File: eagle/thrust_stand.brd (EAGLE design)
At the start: 100 x 80 mm, 28 parts, among them IC1 7805TV, Q1 16Mhz, Q2 IRF510, T1 2N3904, U2 ATMEGA328P_PDIP

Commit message: routed
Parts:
- moved LED1 2.62 mm to (66.7, 34.3), turned to 90 degrees
- moved BATTERY 2.54 mm to (62.2, 48.3)
- moved R2 2.29 mm to (64.1, 27.9)
- moved IGNITER 1.80 mm to (67.3, 12.7), turned to 270 degrees
- moved Q2 1.27 mm to (64.8, 16.5)
- moved R24 1.27 mm to (26.7, 24.1)
- moved BUTTON 1.27 mm to (53.3, 41.9)
- moved R1 0.63 mm to (36.8, 48.9)
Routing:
- net GND: track 63.5 -> 227.3 mm, vias 0 -> 2
- net +5V: track 26.4 -> 129.3 mm, vias 0 -> 2
- net +9V: track 0.00 -> 38.9 mm
- net N$24: track 0.00 -> 17.9 mm
- net N$4: track 0.00 -> 17.3 mm
- net N$5: track 0.00 -> 16.5 mm
- net N$12: track 0.00 -> 12.5 mm
- net N$15: track 0.00 -> 11.2 mm
- net N$3: track 0.00 -> 10.7 mm
- net N$6: track 0.00 -> 10.7 mm
- net N$43: track 0.00 -> 8.35 mm
- net N$13: track 0.00 -> 6.13 mm
- net N$16: track 0.00 -> 5.61 mm
- net N$21: track 0.00 -> 5.46 mm
- net N$14: track 0.00 -> 3.18 mm
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
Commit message: tweaks
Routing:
- net N$7: track 41.8 -> 39.7 mm
- net GND: track 227.3 -> 226.8 mm
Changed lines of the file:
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@@
 <wire x1="30.48" y1="30.48" x2="30.48" y2="33.02" width="0.8128" layer="16"/>
 <wire x1="30.48" y1="33.02" x2="36.83" y2="33.02" width="0.8128" layer="16"/>
-<wire x1="53.34" y1="46.99" x2="55.88" y2="46.99" width="0.8128" layer="16"/>
-<wire x1="55.88" y1="46.99" x2="59.69" y2="43.18" width="0.8128" layer="16"/>
+<wire x1="53.34" y1="46.99" x2="55.88" y2="46.99" width="1.016" layer="16"/>
+<wire x1="55.88" y1="46.99" x2="59.69" y2="43.18" width="1.016" layer="16"/>
 <wire x1="36.83" y1="52.705" x2="21.59" y2="52.705" width="0.8128" layer="16"/>
 <wire x1="21.59" y1="52.705" x2="13.97" y2="45.085" width="0.8128" layer="16"/>
@@
 <wire x1="48.26" y1="31.75" x2="46.99" y2="31.75" width="0.8128" layer="16"/>
 <wire x1="46.99" y1="31.75" x2="43.18" y2="29.21" width="0.8128" layer="16"/>
-<wire x1="43.18" y1="29.21" x2="43.18" y2="12.7" width="0.8128" layer="16"/>
-<wire x1="43.18" y1="12.7" x2="45.72" y2="11.43" width="0.8128" layer="16"/>
+<wire x1="43.18" y1="29.21" x2="43.18" y2="13.97" width="0.8128" layer="16"/>
+<wire x1="43.18" y1="13.97" x2="45.72" y2="11.43" width="0.8128" layer="16"/>
 <wire x1="45.72" y1="11.43" x2="52.07" y2="11.43" width="0.8128" layer="16"/>
 <wire x1="52.07" y1="11.43" x2="55.88" y2="13.97" width="0.8128" layer="16"/>
@@
 <contactref element="IGNITER" pad="TP-2"/>
 <wire x1="43.18" y1="29.21" x2="40.64" y2="29.21" width="0.8128" layer="16"/>
-<wire x1="53.34" y1="49.53" x2="57.15" y2="49.53" width="0.8128" layer="16"/>
-<wire x1="57.15" y1="49.53" x2="60.96" y2="48.26" width="0.8128" layer="16"/>
+<wire x1="53.34" y1="49.53" x2="57.15" y2="49.53" width="1.016" layer="16"/>
+<wire x1="57.15" y1="49.53" x2="60.96" y2="48.26" width="1.016" layer="16"/>
 <wire x1="24.13" y1="16.51" x2="25.4" y2="17.78" width="0.8128" layer="16"/>
 <wire x1="25.4" y1="17.78" x2="29.21" y2="17.78" width="0.8128" layer="16"/>
@@
 <wire x1="27.94" y1="40.64" x2="26.67" y2="39.37" width="0.8128" layer="16"/>
 <wire x1="26.67" y1="39.37" x2="26.67" y2="30.48" width="0.8128" layer="16"/>
-<wire x1="60.96" y1="48.26" x2="60.96" y2="46.355" width="0.8128" layer="16"/>
-<wire x1="60.96" y1="46.355" x2="62.23" y2="45.085" width="0.8128" layer="16"/>
-<wire x1="62.23" y1="45.085" x2="62.23" y2="43.18" width="0.8128" layer="16"/>
-<wire x1="60.96" y1="35.56" x2="60.96" y2="38.1" width="0.8128" layer="16"/>
-<wire x1="60.96" y1="38.1" x2="62.23" y2="39.37" width="0.8128" layer="16"/>
-<wire x1="62.23" y1="39.37" x2="62.23" y2="43.18" width="0.8128" layer="16"/>
-<wire x1="66.675" y1="35.56" x2="60.96" y2="35.56" width="0.8128" layer="16"/>
-<wire x1="54.61" y1="41.91" x2="54.61" y2="39.37" width="0.8128" layer="16"/>
+<wire x1="60.96" y1="48.26" x2="60.96" y2="46.355" width="1.016" layer="16"/>
+<wire x1="60.96" y1="46.355" x2="62.23" y2="45.085" width="1.016" layer="16"/>
+<wire x1="62.23" y1="45.085" x2="62.23" y2="43.18" width="1.016" layer="16"/>
+<wire x1="60.96" y1="35.56" x2="60.96" y2="38.1" width="1.016" layer="16"/>
+<wire x1="60.96" y1="38.1" x2="62.23" y2="39.37" width="1.016" layer="16"/>
+<wire x1="62.23" y1="39.37" x2="62.23" y2="43.18" width="1.016" layer="16"/>
+<wire x1="66.675" y1="35.56" x2="60.96" y2="35.56" width="1.016" layer="16"/>
+<wire x1="54.61" y1="41.91" x2="54.61" y2="39.37" width="1.016" layer="16"/>
 <wire x1="55.88" y1="38.1" x2="55.88" y2="33.02" width="0.8128" layer="16"/>
 <wire x1="55.88" y1="33.02" x2="53.975" y2="31.115" width="0.8128" layer="16"/>
@@
 <wire x1="22.86" y1="22.86" x2="20.32" y2="22.86" width="0.8128" layer="16"/>
 <via x="60.96" y="38.1" extent="1-16" drill="0.8" shape="square"/>
-<wire x1="60.96" y1="38.1" x2="55.88" y2="38.1" width="0.8128" layer="1"/>
+<wire x1="60.96" y1="38.1" x2="55.88" y2="38.1" width="1.016" layer="1"/>
 <via x="55.88" y="38.1" extent="1-16" drill="0.8" shape="square"/>
-<wire x1="55.88" y1="38.1" x2="54.61" y2="39.37" width="0.8128" layer="16"/>
+<wire x1="55.88" y1="38.1" x2="54.61" y2="39.37" width="1.016" layer="16"/>
 <wire x1="67.31" y1="10.795" x2="70.485" y2="10.795" width="0.8128" layer="16"/>
-<wire x1="70.485" y1="10.795" x2="71.755" y2="12.065" width="0.8128" layer="16"/>
-<wire x1="71.755" y1="12.065" x2="71.755" y2="41.275" width="0.8128" layer="16"/>
-<wire x1="71.755" y1="41.275" x2="66.04" y2="51.435" width="0.8128" layer="16"/>
-<wire x1="66.04" y1="51.435" x2="62.23" y2="51.435" width="0.8128" layer="16"/>
-<wire x1="62.23" y1="51.435" x2="60.96" y2="49.53" width="0.8128" layer="16"/>
+<wire x1="70.485" y1="10.795" x2="71.755" y2="12.065" width="1.016" layer="16"/>
+<wire x1="71.755" y1="12.065" x2="71.755" y2="41.275" width="1.016" layer="16"/>
+<wire x1="71.755" y1="41.275" x2="66.04" y2="51.435" width="1.016" layer="16"/>
+<wire x1="66.04" y1="51.435" x2="62.23" y2="51.435" width="1.016" layer="16"/>
+<wire x1="62.23" y1="51.435" x2="60.96" y2="49.53" width="1.016" layer="16"/>
 <wire x1="60.96" y1="49.53" x2="60.96" y2="48.26" width="0.8128" layer="16"/>
 </signal>
@@
 <contactref element="U2" pad="14"/>
 <contactref element="SD_CARD" pad="2"/>
-<wire x1="40.64" y1="13.97" x2="40.64" y2="11.43" width="0.8128" layer="16"/>
-<wire x1="40.64" y1="11.43" x2="43.18" y2="8.89" width="0.8128" layer="16"/>
-<wire x1="43.18" y1="8.89" x2="57.15" y2="8.89" width="0.8128" layer="16"/>
-<wire x1="57.15" y1="8.89" x2="59.69" y2="11.43" width="0.8128" layer="16"/>
-<wire x1="59.69" y1="11.43" x2="59.69" y2="25.4" width="0.8128" layer="16"/>
-<wire x1="59.69" y1="25.4" x2="57.15" y2="26.67" width="0.8128" layer="16"/>
+<wire x1="40.64" y1="13.97" x2="40.64" y2="12.065" width="0.8128" layer="16"/>
+<wire x1="40.64" y1="12.065" x2="43.18" y2="9.525" width="0.8128" layer="16"/>
+<wire x1="43.18" y1="9.525" x2="57.15" y2="9.525" width="0.8128" layer="16"/>
+<wire x1="57.15" y1="9.525" x2="59.055" y2="11.43" width="0.8128" layer="16"/>
+<wire x1="59.055" y1="11.43" x2="59.055" y2="25.4" width="0.8128" layer="16"/>
+<wire x1="59.055" y1="25.4" x2="57.15" y2="26.67" width="0.8128" layer="16"/>
 <wire x1="57.15" y1="26.67" x2="55.88" y2="26.67" width="0.8128" layer="16"/>
 </signal>
@@
 <contactref element="BATTERY" pad="2"/>
 <wire x1="63.5" y1="48.26" x2="63.5" y2="46.99" width="0.8128" layer="16"/>
-<wire x1="63.5" y1="46.99" x2="64.77" y2="45.72" width="0.8128" layer="16"/>
-<wire x1="64.77" y1="45.72" x2="64.77" y2="43.18" width="0.8128" layer="16"/>
-<wire x1="64.77" y1="43.18" x2="64.77" y2="41.91" width="0.8128" layer="16"/>
-<wire x1="64.77" y1="41.91" x2="69.85" y2="37.465" width="0.8128" layer="16"/>
-<wire x1="69.85" y1="37.465" x2="69.85" y2="19.685" width="0.8128" layer="16"/>
-<wire x1="69.85" y1="19.685" x2="66.04" y2="19.685" width="0.8128" layer="16"/>
-<wire x1="66.04" y1="19.685" x2="64.77" y2="20.955" width="0.8128" layer="16"/>
-<wire x1="64.77" y1="20.955" x2="64.77" y2="22.86" width="0.8128" layer="16"/>
+<wire x1="63.5" y1="46.99" x2="64.77" y2="45.72" width="1.016" layer="16"/>
+<wire x1="64.77" y1="45.72" x2="64.77" y2="43.18" width="1.016" layer="16"/>
+<wire x1="64.77" y1="43.18" x2="64.77" y2="41.91" width="1.016" layer="16"/>
+<wire x1="64.77" y1="41.91" x2="69.85" y2="37.465" width="1.016" layer="16"/>
+<wire x1="69.85" y1="37.465" x2="69.85" y2="19.685" width="1.016" layer="16"/>
+<wire x1="69.85" y1="19.685" x2="66.04" y2="19.685" width="1.016" layer="16"/>
+<wire x1="66.04" y1="19.685" x2="64.77" y2="20.955" width="1.016" layer="16"/>
+<wire x1="64.77" y1="20.955" x2="64.77" y2="22.86" width="1.016" layer="16"/>
 </signal>
 <signal name="N$18">
@@
 <contactref element="R2" pad="1"/>
 <contactref element="LED1" pad="A"/>
-<wire x1="66.675" y1="33.02" x2="66.675" y2="29.845" width="0.8128" layer="16"/>
-<wire x1="66.675" y1="29.845" x2="67.945" y2="27.94" width="0.8128" layer="16"/>
+<wire x1="66.675" y1="33.02" x2="66.675" y2="29.845" width="1.016" layer="16"/>
+<wire x1="66.675" y1="29.845" x2="67.945" y2="27.94" width="1.016" layer="16"/>
 </signal>
 <signal name="N$24">
@@
 <contactref element="R2" pad="2"/>
 <contactref element="IGNITER" pad="TP-1"/>
-<wire x1="60.325" y1="27.94" x2="62.23" y2="25.4" width="0.8128" layer="16"/>
-<wire x1="62.23" y1="25.4" x2="62.23" y2="22.86" width="0.8128" layer="16"/>
-<wire x1="62.23" y1="22.86" x2="62.23" y2="15.875" width="0.8128" layer="16"/>
-<wire x1="62.23" y1="15.875" x2="67.31" y2="14.605" width="0.8128" layer="16"/>
+<wire x1="60.325" y1="27.94" x2="62.23" y2="25.4" width="1.016" layer="16"/>
+<wire x1="62.23" y1="25.4" x2="62.23" y2="22.86" width="1.016" layer="16"/>
+<wire x1="62.23" y1="22.86" x2="62.23" y2="15.875" width="1.016" layer="16"/>
+<wire x1="62.23" y1="15.875" x2="67.31" y2="14.605" width="1.016" layer="16"/>
 </signal>
 <signal name="N$12">
 <contactref element="Q2" pad="1"/>
 <contactref element="R5" pad="1"/>
-<wire x1="60.96" y1="33.02" x2="60.96" y2="31.75" width="0.8128" layer="16"/>
-<wire x1="60.96" y1="31.75" x2="66.04" y2="26.67" width="0.8128" layer="16"/>
-<wire x1="66.04" y1="26.67" x2="67.31" y2="22.86" width="0.8128" layer="16"/>
+<wire x1="60.96" y1="33.02" x2="60.96" y2="31.75" width="1.016" layer="16"/>
+<wire x1="60.96" y1="31.75" x2="66.04" y2="26.67" width="1.016" layer="16"/>
+<wire x1="66.04" y1="26.67" x2="67.31" y2="22.86" width="1.016" layer="16"/>
 </signal>
 <signal name="N$3">

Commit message: rotary encoder schemo and codes
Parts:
- added SW1: EC12E_SW, switch-alps:ALPS_EC12E_SW
- moved HX711 25.4 mm to (30.5, 10.2), turned to 0 degrees
- moved I2C_1 5.39 mm to (14.0, 47.0)
- moved RESET 5.08 mm to (31.8, 50.8)
- moved I2C_2 4.58 mm to (14.0, 39.4)
- moved I2C_3 4.02 mm to (14.0, 31.8)
- moved LED1 2.54 mm to (66.7, 36.8)
- moved R3 1.80 mm to (31.8, 16.5)
- moved C1 1.80 mm to (29.2, 26.7)
- moved Q1 1.80 mm to (34.3, 24.1)
- moved R24 1.80 mm to (25.4, 25.4)
- moved C2 1.80 mm to (29.2, 21.6)
- moved C3 1.27 mm to (36.8, 33.0)
- moved T1 1.27 mm to (24.1, 16.5)
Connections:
- new net N$19: SW1.B, U2.4
- new net N$20: SW1.A, U2.5
- new net N$22: SW1.D, U2.6
- net GND: now also SW1.C, SW1.E
- net N$13: now also U2.11; no longer U2.12
- net N$3: now also U2.12; no longer U2.5
- net N$6: now also U2.13; no longer U2.4
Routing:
- net GND: track 226.8 -> 0.00 mm, vias 2 -> 0
- net +5V: track 129.3 -> 0.00 mm, vias 2 -> 0
- net N$1: track 50.4 -> 0.00 mm
- net N$2: track 47.0 -> 0.00 mm
- net N$7: track 39.7 -> 0.00 mm
- net +9V: track 38.9 -> 0.00 mm
- net N$24: track 17.9 -> 0.00 mm
- net N$4: track 17.3 -> 0.00 mm
- net N$5: track 16.5 -> 0.00 mm
- net N$8: track 15.9 -> 0.00 mm, vias 2 -> 0
- net N$12: track 12.5 -> 0.00 mm
- net N$15: track 11.2 -> 0.00 mm
- net N$3: track 10.7 -> 0.00 mm
- net N$6: track 10.7 -> 0.00 mm
- net N$11: track 8.67 -> 0.00 mm
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
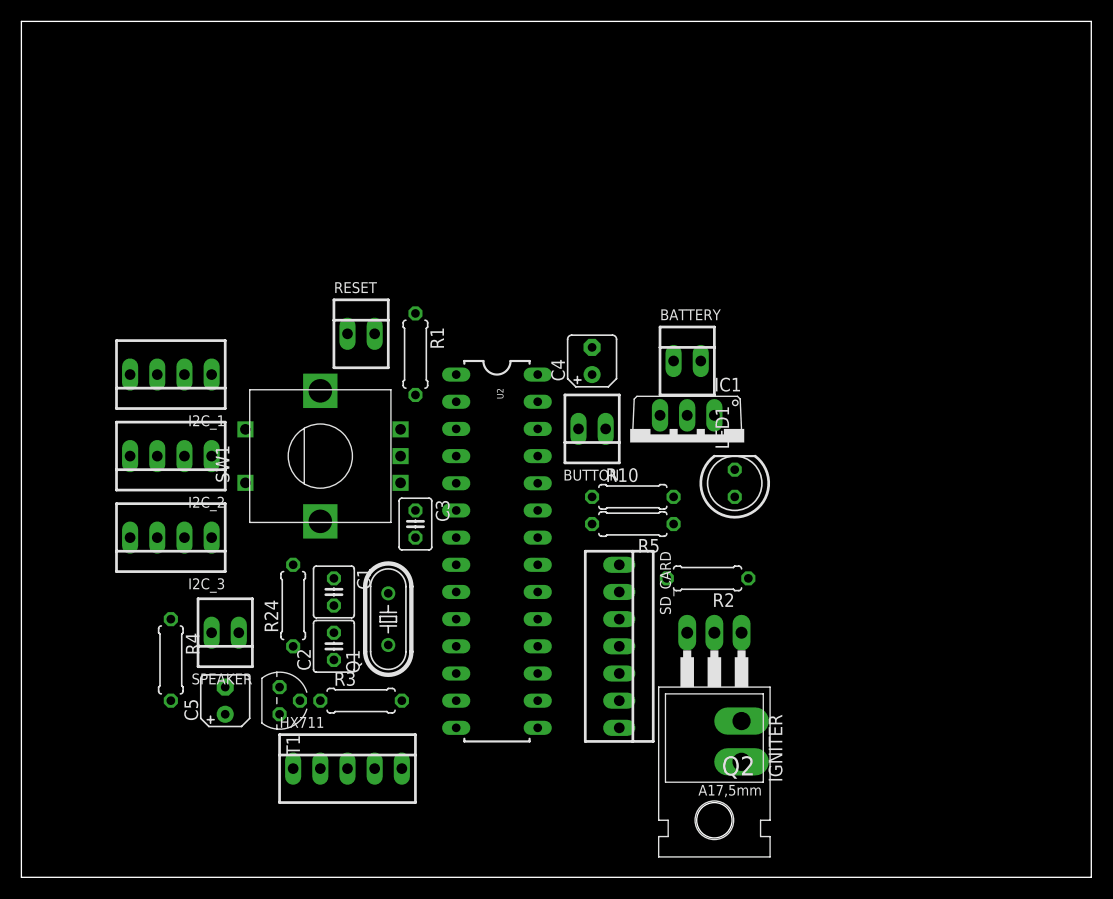
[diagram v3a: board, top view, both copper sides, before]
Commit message: routed with cutout
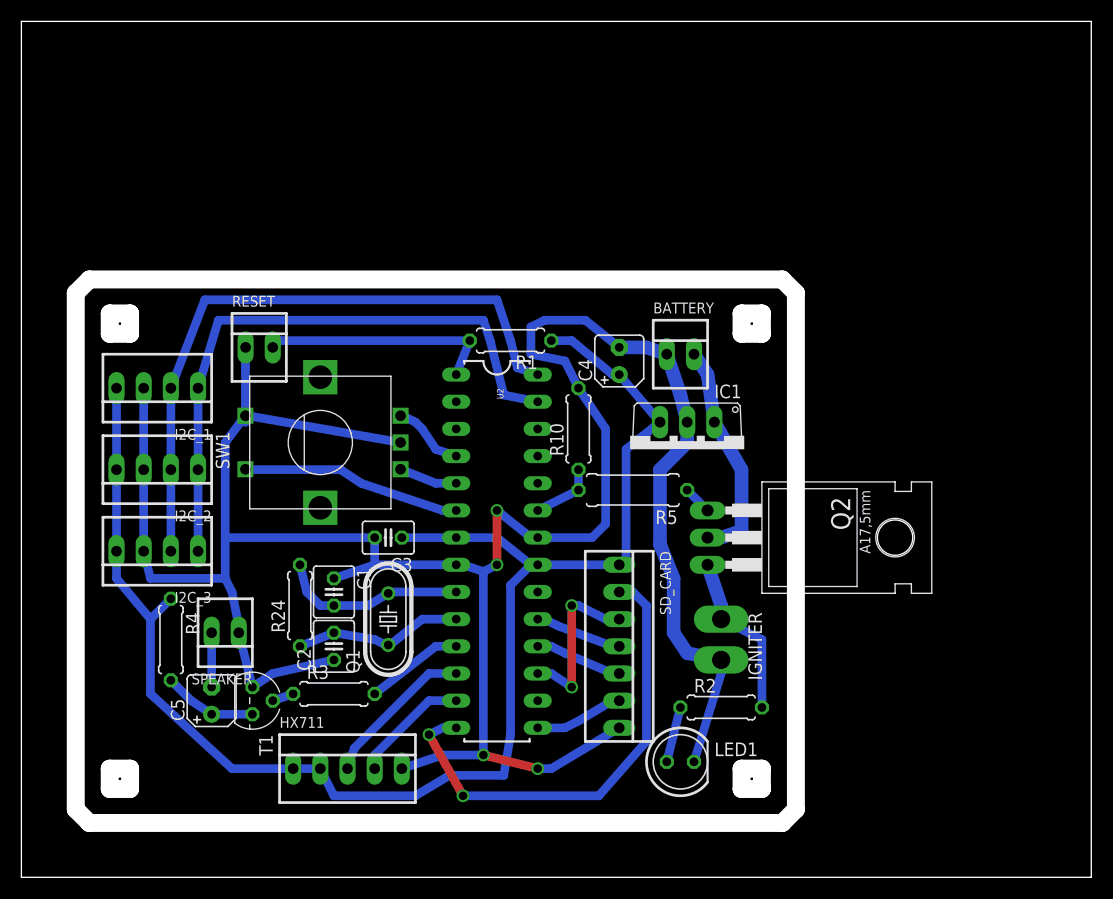
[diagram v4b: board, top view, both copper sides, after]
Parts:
- removed BUTTON: 22-23-2021, con-molex:22-23-2021
- R5: device rcl:0207/7 -> rcl:0309/10
- moved LED1 26.5 mm to (61.6, 10.8), turned to 0 degrees
- moved Q2 16.3 mm to (70.5, 31.8), turned to 270 degrees
- moved R2 12.1 mm to (65.4, 15.9), turned to 0 degrees
- moved IGNITER 9.71 mm to (65.4, 22.2)
- moved RESET 9.61 mm to (22.2, 49.5)
- moved R1 8.98 mm to (45.7, 50.2), turned to 180 degrees
- moved R10 8.13 mm to (52.1, 41.9), turned to 90 degrees
- moved R5 3.17 mm to (57.1, 36.2)
- moved C3 2.84 mm to (34.3, 31.8), turned to 180 degrees
- moved R3 2.62 mm to (29.2, 17.1)
- moved C4 2.54 mm to (55.9, 48.3)
- moved T1 2.54 mm to (21.6, 16.5)
- moved R4 1.91 mm to (14.0, 22.2)
- moved I2C_1 1.80 mm to (12.7, 45.7)
- moved I2C_3 1.80 mm to (12.7, 30.5)
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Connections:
- removed net N$17: BUTTON.2, U2.24
- net GND: no longer BUTTON.1
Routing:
- net GND: track 0.00 -> 248.4 mm, vias 0 -> 4
- net +5V: track 0.00 -> 140.5 mm
- net N$1: track 0.00 -> 60.0 mm
- net N$2: track 0.00 -> 57.1 mm
- net N$7: track 0.00 -> 44.4 mm, vias 0 -> 2
- net N$43: track 0.00 -> 22.1 mm
- net +9V: track 0.00 -> 20.9 mm
- net N$22: track 0.00 -> 20.5 mm
- net N$4: track 0.00 -> 17.6 mm
- net N$5: track 0.00 -> 16.1 mm
- net N$8: track 0.00 -> 15.9 mm, vias 0 -> 2
- net N$24: track 0.00 -> 15.9 mm
- net N$3: track 0.00 -> 14.4 mm
- net N$6: track 0.00 -> 11.0 mm
- net N$13: track 0.00 -> 9.15 mm
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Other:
- outline, holes or cut-outs redrawn

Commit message: igniter moved to supply side and saving calibration value when finished calib
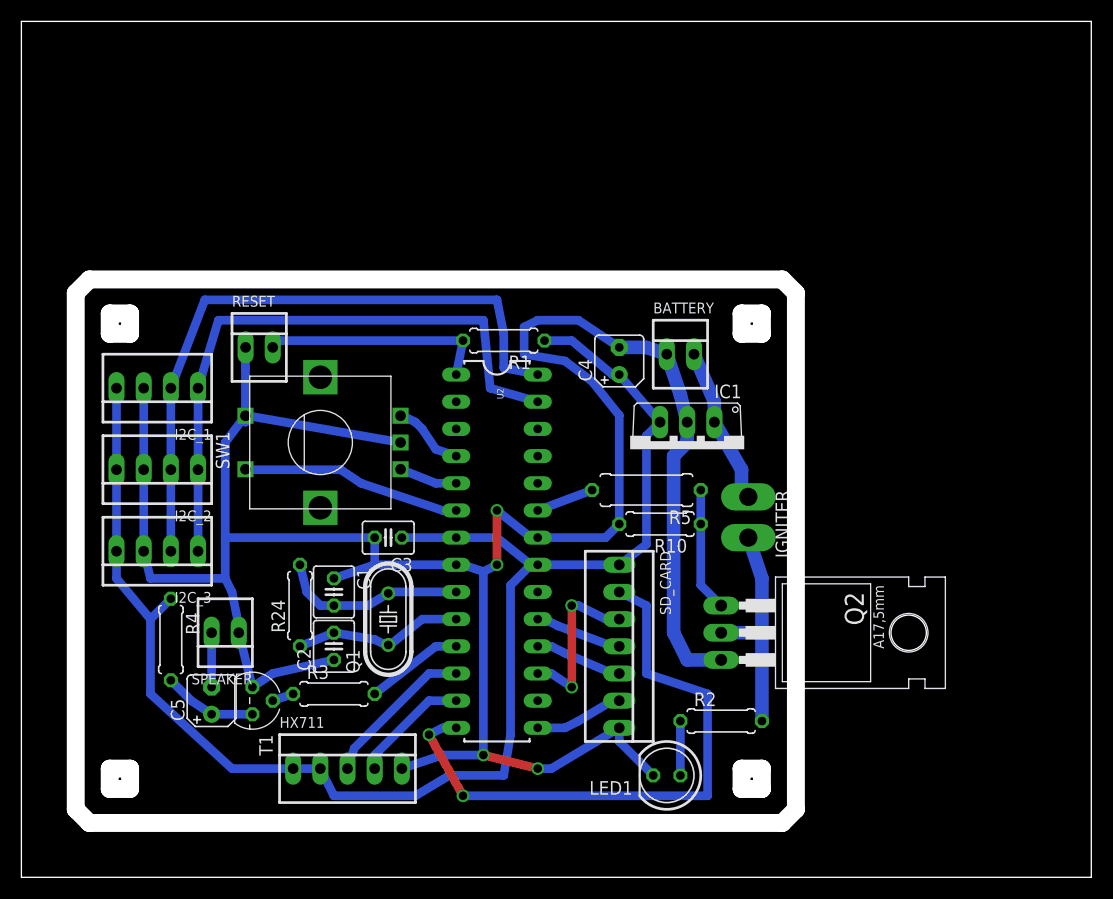
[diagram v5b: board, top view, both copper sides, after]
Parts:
- R2: value 330 -> 1k
- moved IGNITER 11.7 mm to (67.9, 33.7)
- moved R10 11.7 mm to (59.7, 33.0), turned to 180 degrees
- moved Q2 8.98 mm to (71.8, 22.9)
- moved LED1 1.80 mm to (60.3, 9.53), turned to 180 degrees
- moved R5 1.27 mm to (58.4, 36.2)
- moved R2 1.27 mm to (65.4, 14.6)
- moved R1 0.63 mm to (45.1, 50.2)
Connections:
- removed net N$24: IGNITER.TP-1, Q2.3, R2.2
- new net N$17: IGNITER.TP-2, Q2.2, R2.2
- net +9V: now also IGNITER.TP-1; no longer Q2.2
- net GND: now also Q2.3; no longer IGNITER.TP-2
- net N$12: now also R10.1
- net N$18: no longer R10.1
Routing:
- net N$17: track 0.00 -> 21.8 mm
- net N$24: track 15.9 -> 0.00 mm
- net N$7: track 44.4 -> 56.8 mm
- net N$12: track 2.69 -> 11.6 mm
- net +9V: track 20.9 -> 13.8 mm
- net N$1: track 60.0 -> 61.0 mm
- net GND: track 248.4 -> 247.5 mm
- net N$43: track 22.1 -> 21.3 mm
- net N$18: track 6.16 -> 5.43 mm
- net +5V: track 140.5 -> 141.1 mm
- net N$2: track 57.1 -> 57.6 mm
